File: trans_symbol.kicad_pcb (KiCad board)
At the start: 2 copper layers, 81.7 x 93.6 mm, 111 parts, among them J3 USB_B_Micro, U1 ATSAMD21G18A-AU, U2 MIC5504-3.3YM5, Y1 32768Hz

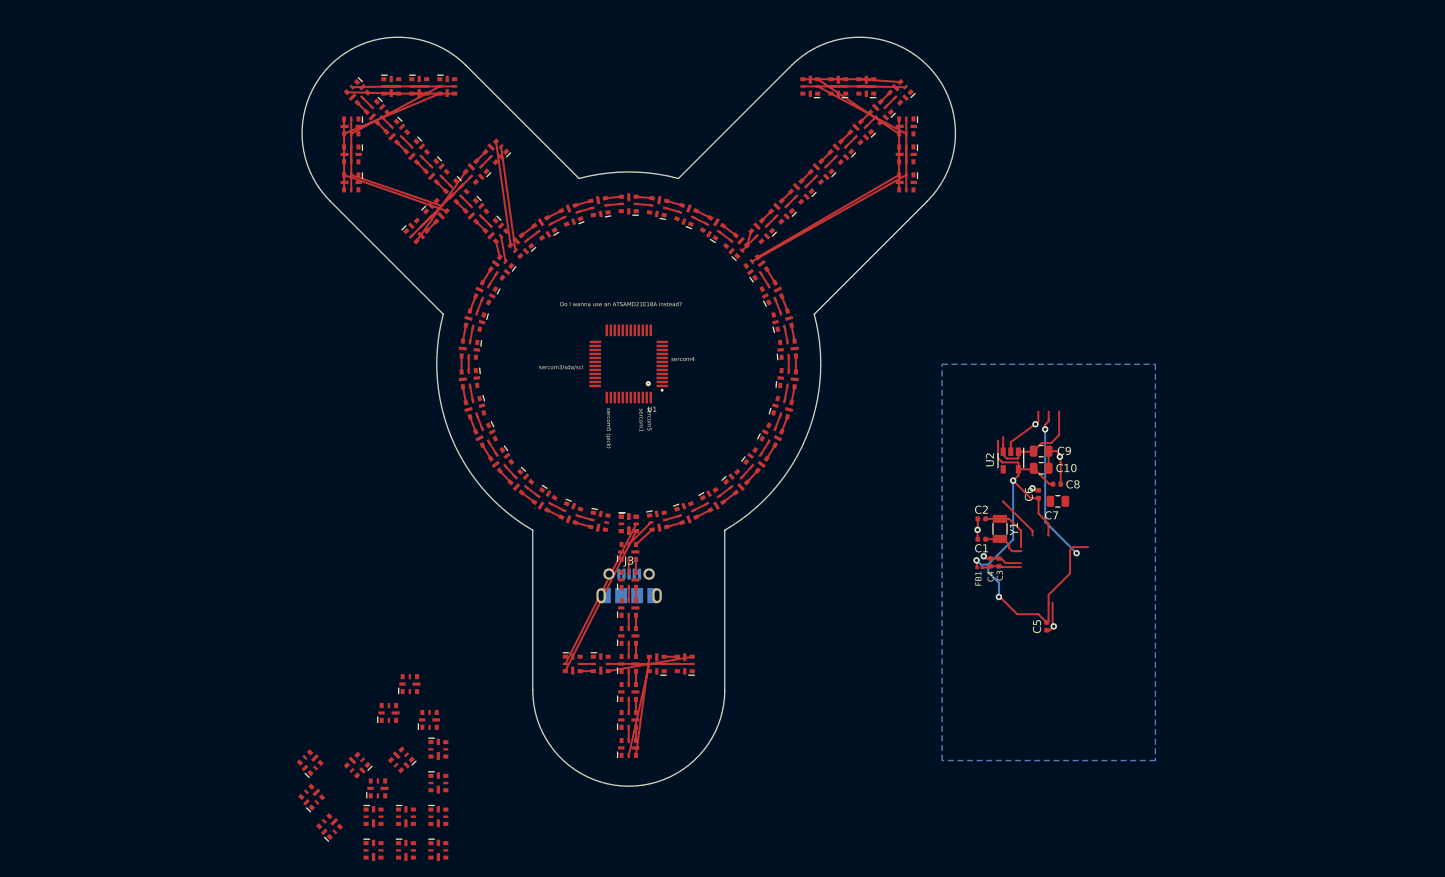
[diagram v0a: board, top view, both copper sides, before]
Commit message: fix pixel orientation on arrow; add via for GND out of each LED (we cannot delete vias programmatically due to a crasher, so layout is manual from here on out); choose pins for SPI; wire up SPI & USB data
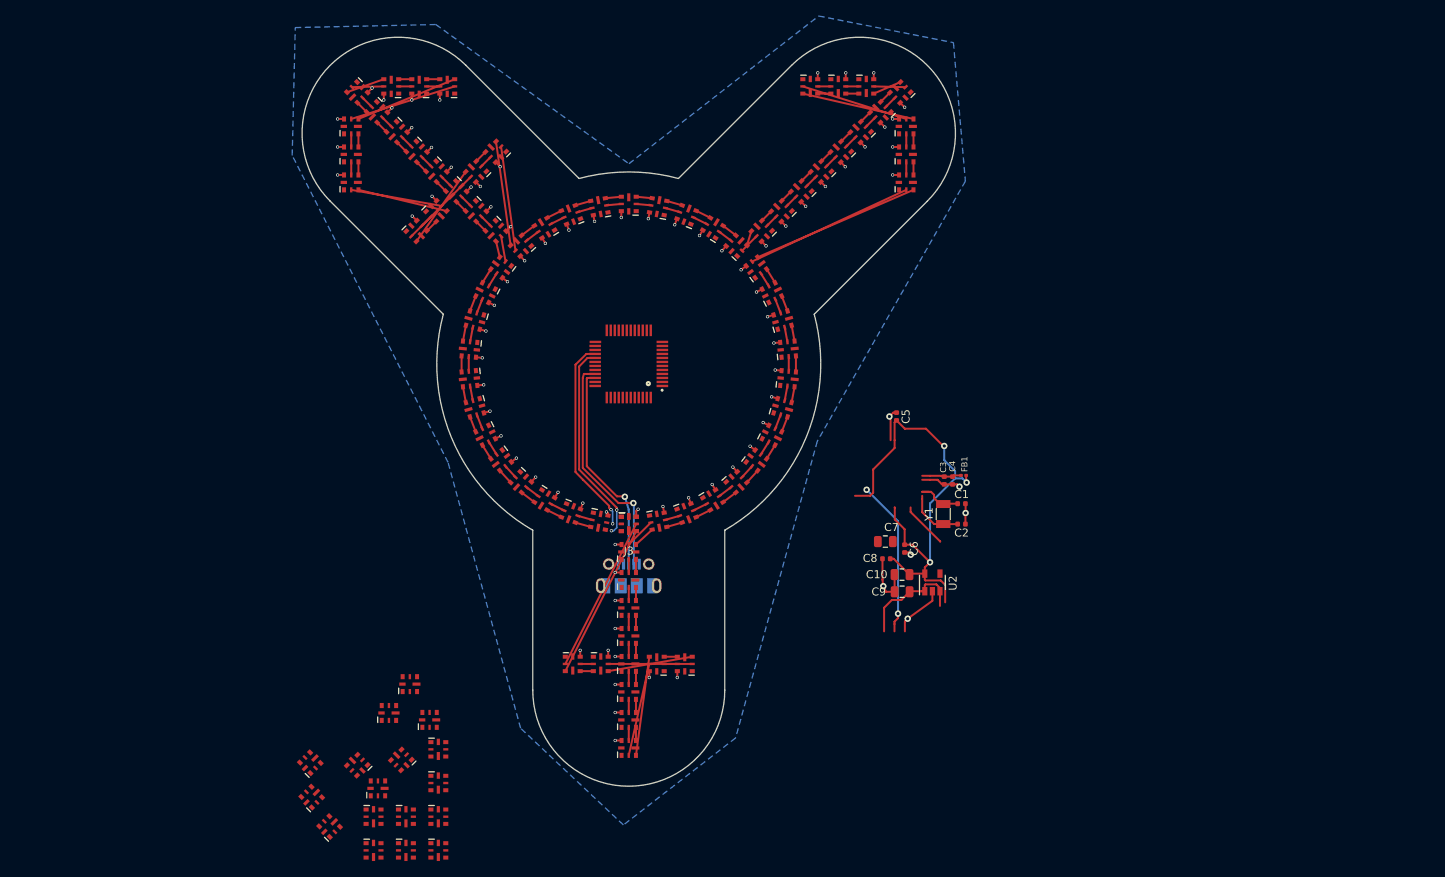
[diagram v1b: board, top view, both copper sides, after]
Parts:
- moved C5 32.3 mm to (123.5, 96.6), turned to 270 degrees
- moved C9 24.7 mm to (124.2, 118.5), turned to 180 degrees
- moved C8 23.3 mm to (122.2, 114.4), turned to 180 degrees
- moved C7 22.1 mm to (122.1, 112.2), turned to 180 degrees
- moved C10 21.9 mm to (124.2, 116.3), turned to 180 degrees
- moved U2 18.1 mm to (128.0, 117.3), turned to 90 degrees
- moved C6 18.1 mm to (124.5, 113.1), turned to 270 degrees
- moved C3 12.3 mm to (129.4, 104.6), turned to 270 degrees
- moved FB1 11.7 mm to (131.9, 103.9), turned to 180 degrees
- moved C4 11.3 mm to (130.5, 104.6), turned to 90 degrees
- moved Y1 7.33 mm to (129.3, 108.8), turned to 270 degrees
- moved C1 5.11 mm to (131.6, 107.5), turned to 0 degrees
- moved C2 2.60 mm to (131.6, 110.0), turned to 0 degrees
- moved J3 1.25 mm to (90.0, 116.5)
- turned D21 to 180 degrees
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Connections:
- net PA17 renamed PA17_MISO
- D1 pad 4: /Sheet5F81AC31/LED_DATA -> PA20_MOSI
- D1 pad 5: /Sheet5F81AC31/LED_SCK -> PA19_SCK
- U1 pad 28: PA19 -> PA19_SCK
- U1 pad 29: PA20 -> PA20_MOSI
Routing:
- net GND: track 26.7 -> 89.1 mm, vias 6 -> 84
- net USB_D-: track 0.00 -> 29.0 mm, vias 0 -> 1
- net USB_D+: track 19.5 -> 46.4 mm, vias 2 -> 3
- net PA20_MOSI: track 0.00 -> 25.5 mm, vias 0 -> 2
- net PA19_SCK: track 0.00 -> 24.8 mm, vias 0 -> 2
- net Net-(D49-Pad3): track 5.36 -> 1.64 mm
- net Net-(D49-Pad2): track 5.36 -> 1.64 mm
- net Net-(D48-Pad3): track 5.36 -> 1.64 mm
- net Net-(D48-Pad2): track 5.36 -> 1.64 mm
- net Net-(D52-Pad3): track 5.36 -> 1.64 mm
- net Net-(D52-Pad2): track 5.36 -> 1.64 mm
- net Net-(D51-Pad3): track 5.36 -> 1.64 mm
- net Net-(D51-Pad2): track 5.36 -> 1.64 mm
- net Net-(D25-Pad3): track 5.36 -> 1.64 mm
- net Net-(D25-Pad2): track 5.36 -> 1.64 mm
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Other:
- rule via_min_drill: 0.3 -> 0.254
- board text removed: "Do I wanna use an ATSAMD21E18A instead?"
- board text removed: "sercom1"
- board text removed: "sercom3/sda/scl"
- board text removed: "sercom4"
- board text removed: "sercom5"
- board text removed: "sercom5 (pick)"

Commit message: first pass on manual layout of board including led power traces & samd circuitry; key idea: take out the usb port and solder the usb data & power directly to the board, i.e. it'll have its own cable attached, possibly a short cable with the usb plug on it so that I can use various length usb cables
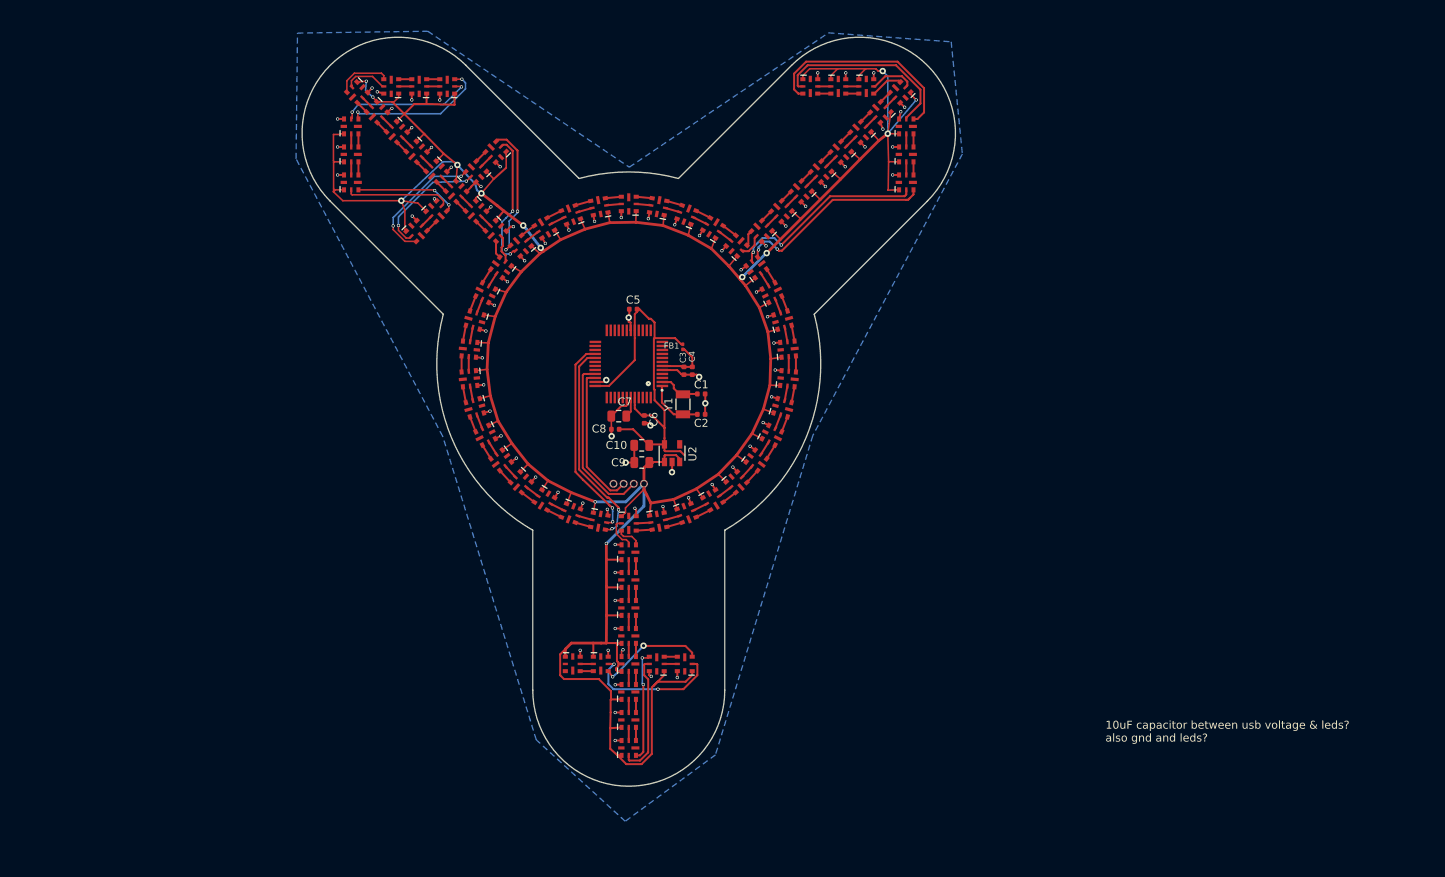
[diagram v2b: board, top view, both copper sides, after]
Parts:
- removed D79, D80, D81, D82, D83, D84, D85, D86, D87, D88, D89, D90, D91, D92, D93, D94, D95, D96: APA102-2020, LED_SMD:LED-APA102-2020_tightened_pads
- removed J3: USB_B_Micro, Connector_USB:USB_Micro-B_Molex-105017-0001
- added J4: Conn_01x04, Connector_PinHeader_1.27mm:PinHeader_1x04_P1.27mm_Vertical, F.Cu at (88.1, 105.0)
- moved FB1 38.6 mm to (96.7, 87.9), turned to 270 degrees
- moved C8 37.5 mm to (88.3, 98.2)
- moved C7 36.8 mm to (88.7, 96.5)
- moved C9 36.3 mm to (91.6, 102.3)
- moved C6 36.3 mm to (91.9, 96.9)
- moved U2 36.3 mm to (95.4, 101.2)
- moved C10 36.3 mm to (91.6, 100.2)
- moved C5 35.5 mm to (90.6, 83.2), turned to 0 degrees
- moved C3 35.3 mm to (96.9, 90.9)
- moved C4 35.3 mm to (97.9, 90.9)
- moved C1 35.3 mm to (99.1, 93.8)
- moved C2 35.3 mm to (99.1, 96.3)
- moved Y1 35.3 mm to (96.8, 95.0)
- moved D78 18.8 mm to (83.0, 127.5)
- moved D74 11.1 mm to (90.0, 138.0), turned to 90 degrees
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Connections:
- net Net-(C3-Pad1) renamed /VDDANA
- net Net-(C7-Pad1) renamed /VDDCORE
- net PA02 renamed Net-(U1-Pad3)
- net PA03 renamed Net-(U1-Pad4)
- net PA04 renamed Net-(U1-Pad9)
- net PA05 renamed Net-(U1-Pad10)
- net PA06 renamed Net-(U1-Pad11)
- net PA07 renamed Net-(U1-Pad12)
- net PA08 renamed Net-(U1-Pad13)
- net PA09 renamed Net-(U1-Pad14)
- net PA10 renamed Net-(U1-Pad15)
- net PA11 renamed Net-(U1-Pad16)
- net PA12 renamed Net-(U1-Pad21)
- net PA13 renamed Net-(U1-Pad22)
- net PA14 renamed Net-(U1-Pad23)
- net PA15 renamed Net-(U1-Pad24)
- net PA16 renamed Net-(U1-Pad25)
- net PA17_MISO renamed /PA17_MISO
- net PA18 renamed Net-(U1-Pad27)
- net PA19_SCK renamed /APA102c LED Array/LED_SCK
- net PA20_MOSI renamed /APA102c LED Array/LED_DATA
- net PA21 renamed Net-(U1-Pad30)
- net PA22 renamed Net-(U1-Pad31)
- net PA23 renamed Net-(U1-Pad32)
- net PA27 renamed Net-(U1-Pad39)
- net PA28 renamed Net-(U1-Pad41)
- net PA30 renamed Net-(U1-Pad45)
- net PA31 renamed Net-(U1-Pad46)
- net PB02 renamed Net-(U1-Pad47)
- net PB03 renamed Net-(U1-Pad48)
- net PB08 renamed Net-(U1-Pad7)
- net PB09 renamed Net-(U1-Pad8)
- net PB10 renamed Net-(U1-Pad19)
- net PB11 renamed Net-(U1-Pad20)
- net PB22 renamed Net-(U1-Pad37)
- net PB23 renamed Net-(U1-Pad38)
- C9 pad 1: VBUS -> +5V
- U1 pad 33: USB_D- -> /USB_D-
- U1 pad 34: USB_D+ -> /USB_D+
- U2 pad 1: VBUS -> +5V
- U2 pad 3: VBUS -> +5V
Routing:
- net +5V: track 0.00 -> 435.0 mm, vias 0 -> 14
- net USB_D+: track 46.4 -> 0.00 mm, vias 3 -> 0
- net USB_D-: track 29.0 -> 0.00 mm, vias 1 -> 0
- net /USB_D-: track 0.00 -> 21.5 mm
- net /USB_D+: track 0.00 -> 18.3 mm
- net Net-(D77-Pad3): track 19.6 -> 1.64 mm
- net Net-(D77-Pad2): track 19.6 -> 1.64 mm
- net Net-(D76-Pad2): track 1.64 -> 17.6 mm, vias 0 -> 2
- net VBUS: track 14.6 -> 0.00 mm
- net Net-(D74-Pad2): track 1.64 -> 15.3 mm
- net Net-(D74-Pad3): track 1.64 -> 13.8 mm, vias 0 -> 2
- net Net-(D50-Pad3): track 14.2 -> 26.2 mm
- net Net-(D76-Pad3): track 1.64 -> 13.3 mm, vias 0 -> 2
- net Net-(D73-Pad3): track 12.4 -> 1.64 mm
- net Net-(D73-Pad2): track 11.7 -> 1.64 mm
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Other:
- board text added: "10uF capacitor between usb voltage & leds? also gnd and leds?"

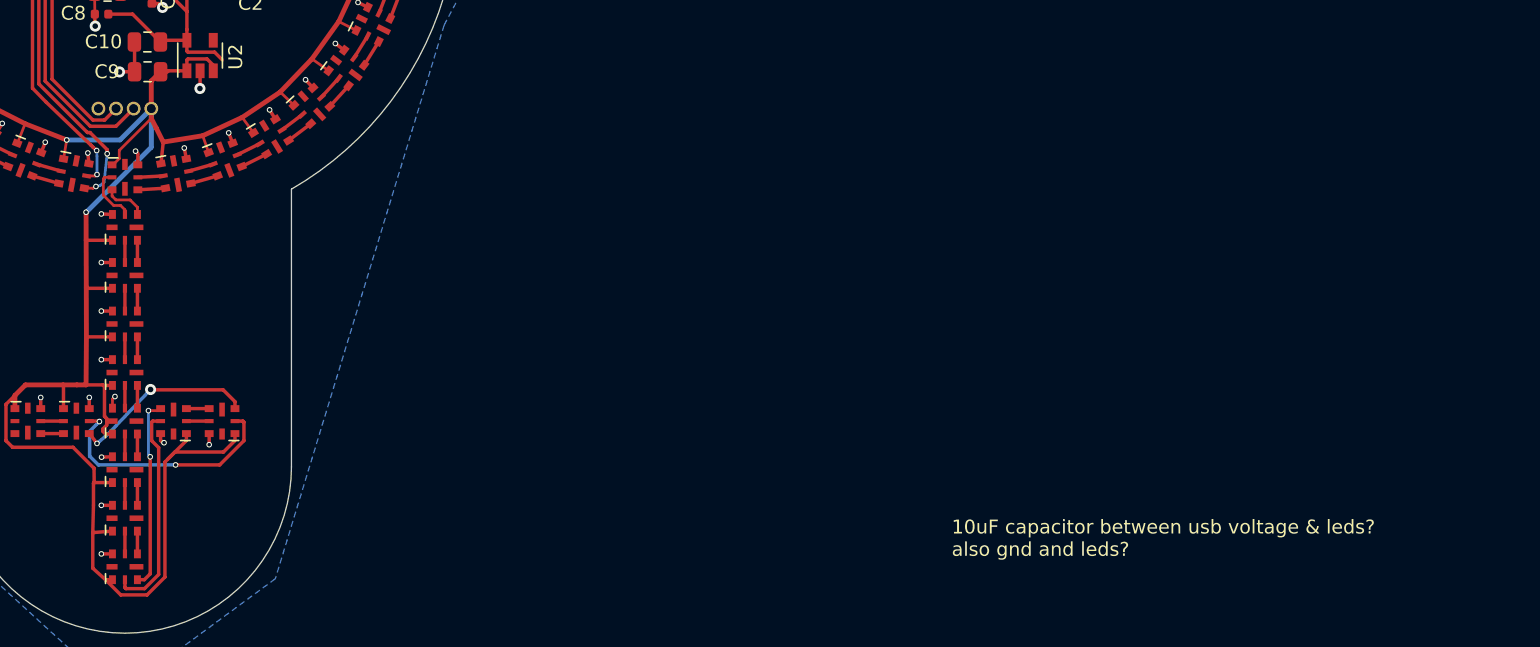
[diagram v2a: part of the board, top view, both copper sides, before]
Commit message: add a decoupling capacitor on +5V for LEDs
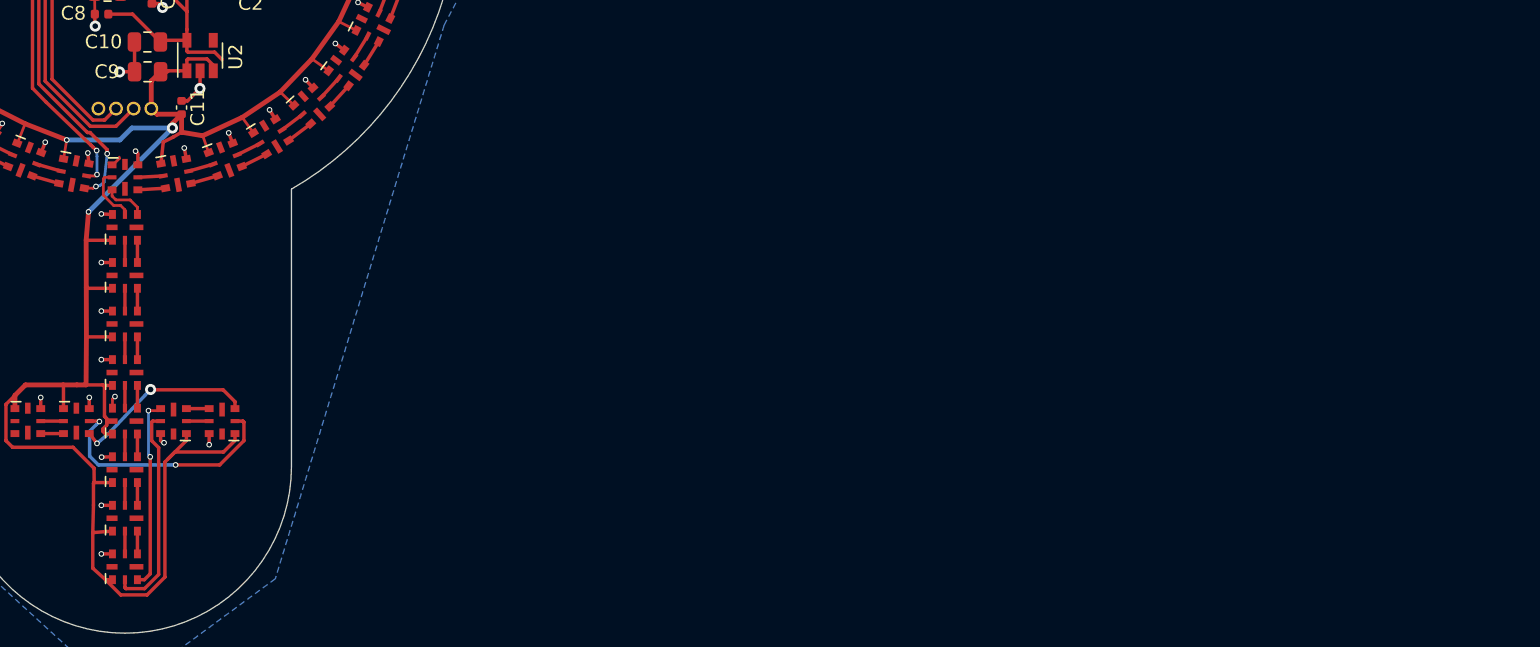
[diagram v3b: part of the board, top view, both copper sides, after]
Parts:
- added C11: 10µF, Capacitor_SMD:C_0402_1005Metric, F.Cu at (94.1, 104.9)
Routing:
- net GND: track 87.1 -> 88.8 mm
- net +5V: track 435.0 -> 433.8 mm, vias 14 -> 15
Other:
- board text removed: "10uF capacitor between usb voltage & leds? also gnd and leds?"
